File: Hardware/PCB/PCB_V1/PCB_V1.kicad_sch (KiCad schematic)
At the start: 33 parts, among them J1 Conn_01x03, J1_Afficheur Conn_01x10, J2 Conn_01x03, J3 Conn_ST_STDC14, J4 Conn_01x02, J5 Conn_01x02, J6 DIN-5_180degree, J7 Conn_01x07, U1 STM32G431KBTx, U2 MCP6002-xSN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

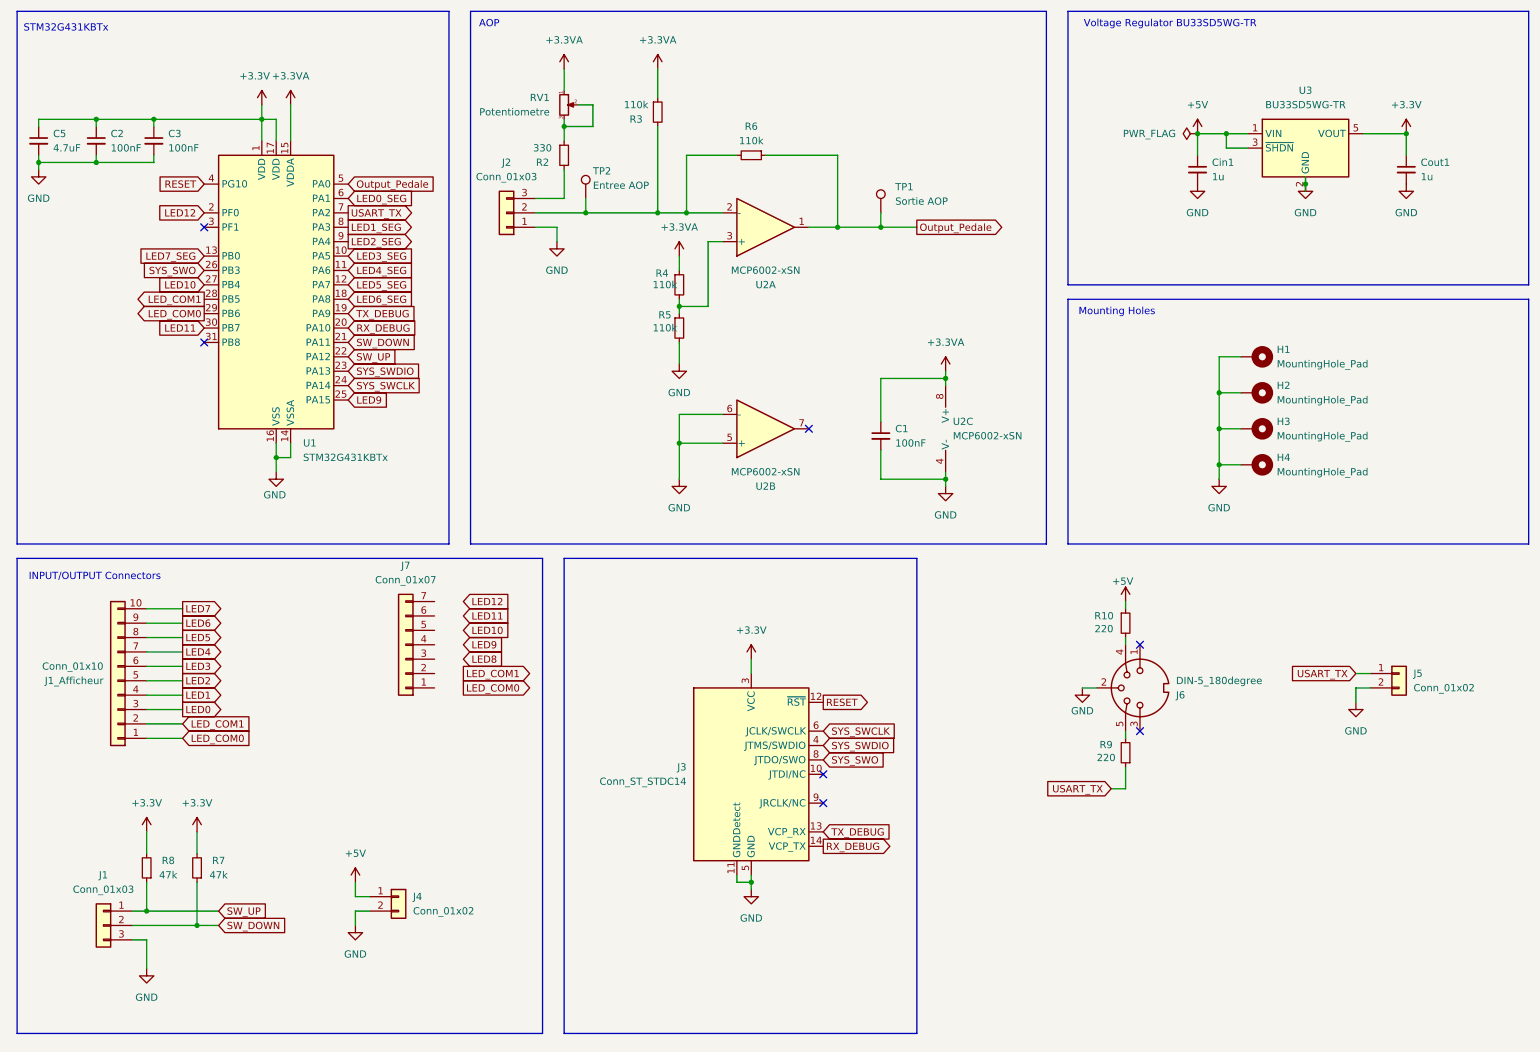
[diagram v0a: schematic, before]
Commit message: ajout transistors LED
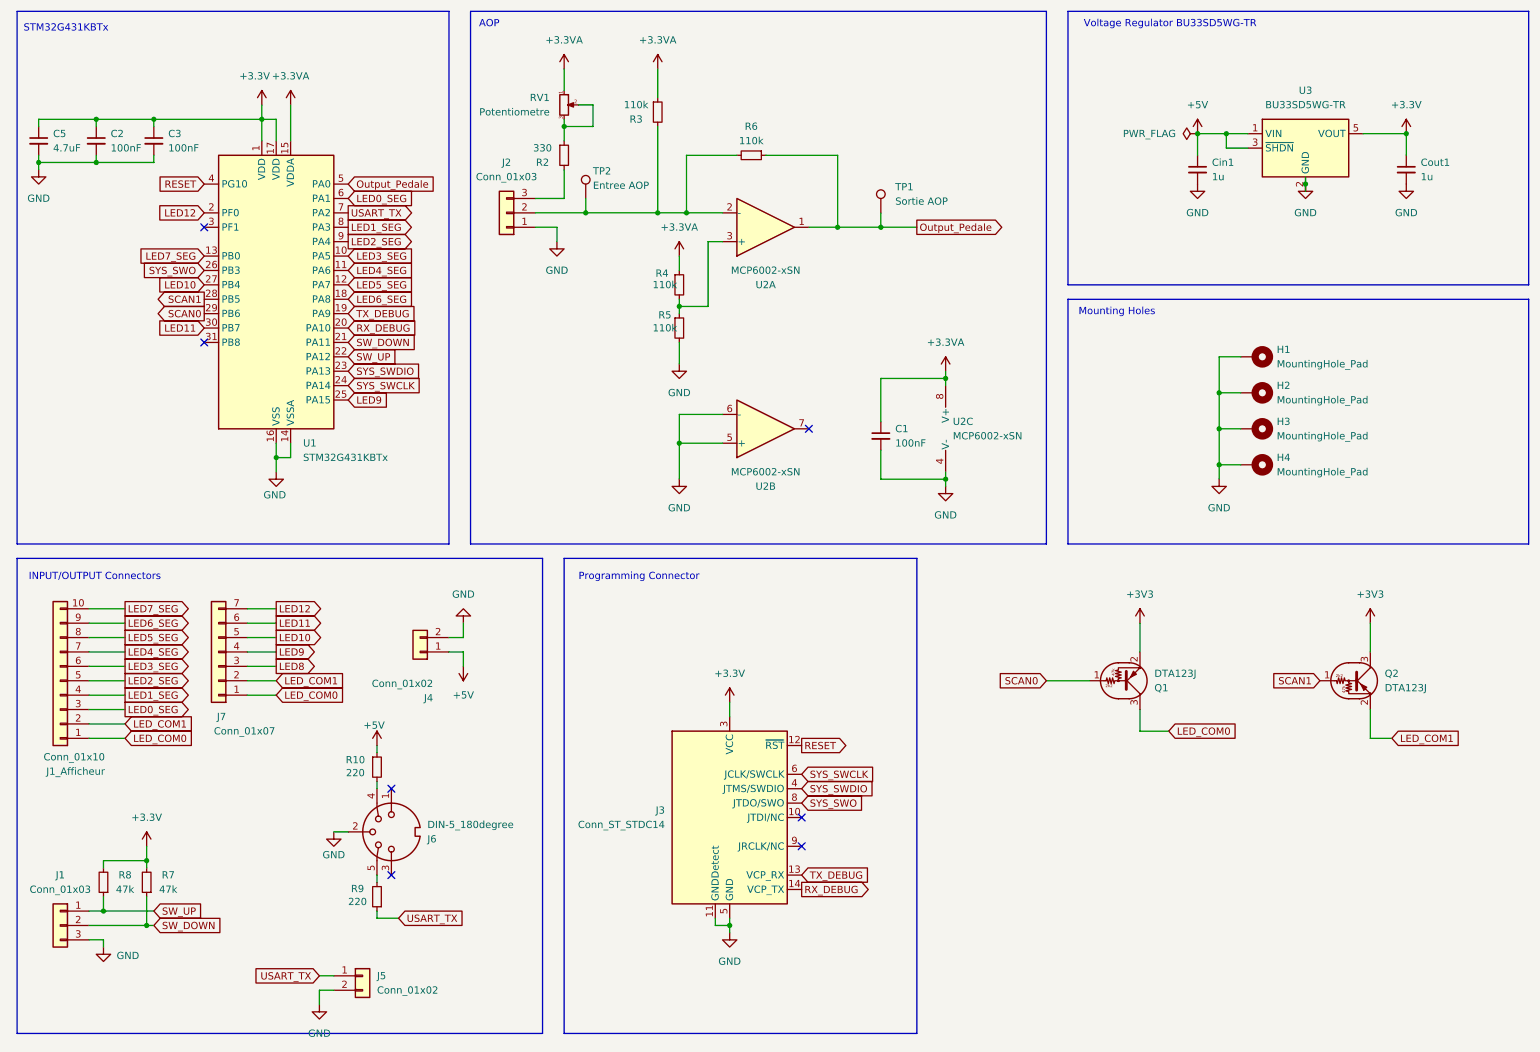
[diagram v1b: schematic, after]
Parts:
- added Q1, Q2: DTA123J, symbol Transistor_BJT:DTA123J
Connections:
- net LED0 is gone; now on net LED0_SEG: J1_Afficheur.3 (Pin_3)
- net LED1 is gone; now on net LED1_SEG: J1_Afficheur.4 (Pin_4)
- net LED2 is gone; now on net LED2_SEG: J1_Afficheur.5 (Pin_5)
- net LED3 is gone; now on net LED3_SEG: J1_Afficheur.6 (Pin_6)
- net LED4 is gone; now on net LED4_SEG: J1_Afficheur.7 (Pin_7)
- net LED5 is gone; now on net LED5_SEG: J1_Afficheur.8 (Pin_8)
- net LED6 is gone; now on net LED6_SEG: J1_Afficheur.9 (Pin_9)
- net LED7 is gone; now on net LED7_SEG: J1_Afficheur.10 (Pin_10)
- net LED10: now also J7.5 (Pin_5)
- net LED11: now also J7.6 (Pin_6)
- net LED12: now also J7.7 (Pin_7)
- net LED8: now also J7.3 (Pin_3)
- net LED9: now also J7.4 (Pin_4)
- net LED_COM0: now also J7.1 (Pin_1), Q1.3 (C); no longer U1.29 (PB6)
- net LED_COM1: now also J7.2 (Pin_2), Q2.2 (E); no longer U1.28 (PB5)
- new net +3V3: Q1.2 (E), Q2.3 (C)
- new net SCAN0: Q1.1 (B), U1.29 (PB6)
- new net SCAN1: Q2.1 (B), U1.28 (PB5)
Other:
- note added: "Programming Connector"
- moved on the sheet: J1, J1_Afficheur, J3, J4, J5, J6, J7, R10, R7, R8, R9

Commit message: Mis à jour schématique
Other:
- note added: "Transistors"
- company: (none) -> ENSEA
- title: (none) -> 1A1B Projet Pedale
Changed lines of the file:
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@@
 	(generator_version "8.0")
 	(paper "A4")
+	(title_block
+		(title "1A1B Projet Pedale")
+		(date "2025-03-11")
+		(rev "1.0")
+		(company "ENSEA")
+		(comment 1 "CHERIFI Sacha")
+		(comment 2 "TURGUT Iprahim")
+		(comment 3 "PREVOST Alexian")
+	)
 	(junction
 		(at 140.97 176.53)
@@
 		)
 	)
+	(rectangle
+		(start 177.8 111.76)
+		(end 275.59 161.29)
+		(stroke
+			(width 0)
+			(type default)
+		)
+		(fill
+			(type none)
+		)
+	)
 	(text "AOP\n"
 		(exclude_from_sim no)
@@
 		)
 	)
+	(text "Transistors"
+		(exclude_from_sim no)
+		(at 184.15 114.046 0)
+		(effects
+			(font
+				(size 1.27 1.27)
+			)
+		)
+	)
 	(text "Programming Connector\n"
 		(exclude_from_sim no)
@@
 		)
 		(instances
-			(project ""
+			(project "PCB_V1"
 				(path "/56432b71-0851-4531-93d8-c32e80e88a85"
 					(reference "#PWR024")
@@
 		)
 		(instances
-			(project ""
+			(project "PCB_V1"
 				(path "/56432b71-0851-4531-93d8-c32e80e88a85"
 					(reference "#PWR025")
@@
 		)
 		(instances
-			(project ""
+			(project "PCB_V1"
 				(path "/56432b71-0851-4531-93d8-c32e80e88a85"
 					(reference "Q1")
@@
 		)
 		(instances
-			(project ""
+			(project "PCB_V1"
 				(path "/56432b71-0851-4531-93d8-c32e80e88a85"
 					(reference "J7")
@@
 		)
 		(instances
-			(project ""
+			(project "PCB_V1"
 				(path "/56432b71-0851-4531-93d8-c32e80e88a85"
 					(reference "#PWR027")
@@
 		)
 		(instances
-			(project ""
+			(project "PCB_V1"
 				(path "/56432b71-0851-4531-93d8-c32e80e88a85"
 					(reference "C2")
@@
 		)
 		(instances
-			(project ""
+			(project "PCB_V1"
 				(path "/56432b71-0851-4531-93d8-c32e80e88a85"
 					(reference "#PWR026")
@@
 		)
 		(instances
-			(project ""
+			(project "PCB_V1"
 				(path "/56432b71-0851-4531-93d8-c32e80e88a85"
 					(reference "TP1")
@@
 		)
 		(instances
-			(project ""
+			(project "PCB_V1"
 				(path "/56432b71-0851-4531-93d8-c32e80e88a85"
 					(reference "#PWR010")
@@
 		)
 		(instances
-			(project ""
+			(project "PCB_V1"
 				(path "/56432b71-0851-4531-93d8-c32e80e88a85"
 					(reference "#PWR020")
@@
 		)
 		(instances
-			(project ""
+			(project "PCB_V1"
 				(path "/56432b71-0851-4531-93d8-c32e80e88a85"
 					(reference "J3")
@@
 		)
 		(instances
-			(project ""
+			(project "PCB_V1"
 				(path "/56432b71-0851-4531-93d8-c32e80e88a85"
 					(reference "#PWR023")
@@
 		)
 		(instances
-			(project ""
+			(project "PCB_V1"
 				(path "/56432b71-0851-4531-93d8-c32e80e88a85"
 					(reference "J4")
@@
 		)
 		(instances
-			(project ""
+			(project "PCB_V1"
 				(path "/56432b71-0851-4531-93d8-c32e80e88a85"
 					(reference "J6")
@@
 		)
 		(instances
-			(project ""
+			(project "PCB_V1"
 				(path "/56432b71-0851-4531-93d8-c32e80e88a85"
 					(reference "RV1")
@@
 		)
 		(instances
-			(project ""
+			(project "PCB_V1"
 				(path "/56432b71-0851-4531-93d8-c32e80e88a85"
 					(reference "#PWR09")
@@
 		)
 		(instances
-			(project ""
+			(project "PCB_V1"
 				(path "/56432b71-0851-4531-93d8-c32e80e88a85"
 					(reference "J1")

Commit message: ajout library footprint DIN5
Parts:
- added C5: 1uF, Capacitor_SMD:C_0603_1608Metric, symbol Device:C_Small
- added C6: 10nF, Capacitor_SMD:C_0402_1005Metric, symbol Device:C_Small
- added H5, H6: MountingHole_Pad, MountingHole:MountingHole_4mm_Pad_TopBottom, symbol Mechanical:MountingHole_Pad
- added L1: 39n, Inductor_SMD:L_0603_1608Metric, symbol Device:L_Small
- C1: footprint (none) -> Capacitor_SMD:C_0402_1005Metric
- C2: renamed from C5; footprint (none) -> Capacitor_SMD:C_0603_1608Metric
- C3: renamed from C2; footprint (none) -> Capacitor_SMD:C_0402_1005Metric
- C4: renamed from C3; footprint (none) -> Capacitor_SMD:C_0402_1005Metric
- Cin1, Cout1: value 1u -> 1uF; footprint (none) -> Capacitor_SMD:C_0603_1608Metric
- H1, H2, H3, H4: footprint (none) -> MountingHole:MountingHole_4mm_Pad_TopBottom
- J1, J2: footprint (none) -> Connector_JST:JST_XH_B3B-XH-A_1x03_P2.50mm_Vertical
- J4, J5: footprint Connector_JST:JST_XH_S2B-XH-A_1x02_P2.50mm_Horizontal -> Connector_JST:JST_XH_B2B-XH-A_1x02_P2.50mm_Vertical
- J7: footprint (none) -> Connector_JST:JST_XH_B7B-XH-A_1x07_P2.50mm_Vertical
- J8_afficheur1: renamed from J1_Afficheur; footprint (none) -> Connector_JST:JST_XH_B10B-XH-A_1x10_P2.50mm_Vertical
- Q1, Q2: footprint (none) -> Package_TO_SOT_SMD:SOT-23-3
- R10, R2, R3, R4, R5, R6, R7, R8, R9: footprint (none) -> Resistor_SMD:R_0402_1005Metric
- RV1: value Potentiometre -> 470; footprint (none) -> Potentiometer_SMD:Potentiometer_Bourns_3314J_Vertical
- U2: footprint (none) -> Package_SO:SOIC-8_3.9x4.9mm_P1.27mm
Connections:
- net +3.3V: now also L1.1
- net +3.3VA: now also C5.1, C6.1, L1.2
- net +3V3: now also Q2.2 (E); no longer Q2.3 (C)
- net GND: now also C5.2, C6.2, H5.1, H6.1
- net LED_COM1: now also Q2.3 (C); no longer Q2.2 (E)
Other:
- moved on the sheet: C2, C3, C4, Cin1, Cout1, H1, H2, H3, H4, J3, J5, Q1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

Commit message: pcb complet
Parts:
- removed H6: MountingHole_Pad, MountingHole:MountingHole_4mm_Pad_TopBottom, symbol Mechanical:MountingHole_Pad
- removed J6: DIN-5_180degree, symbol Connector:DIN-5_180degree
- added D1, D2: LED, LED_SMD:LED_0603_1608Metric, symbol Device:LED
- added J8: PRT-09536, symbol PRT-09536:PRT-09536
- added JP1: SolderJumper1, Jumper:SolderJumper-2_P1.3mm_Open_TrianglePad1.0x1.5mm, symbol Jumper:SolderJumper_2_Open
- added JP2: SolderJumper, Jumper:SolderJumper-2_P1.3mm_Open_TrianglePad1.0x1.5mm, symbol Jumper:SolderJumper_2_Open
- added R1, R11: 1000, Resistor_SMD:R_0402_1005Metric, symbol Device:R_Small
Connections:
- net +3V3 is gone; now on net +3.3V: Q1.2 (E), Q2.2 (E)
- net +3.3V: now also D1.2 (A)
- net +5V: now also R10.2; no longer R10.1
- net GND: now also J8.2, J8.E1, J8.E2, R1.1, R11.1
- net at R9.2: now also JP2.1 (A)
- net at U1.31 (PB8): now also D2.2 (A)
- new net: J8.4, JP1.1 (A)
- new net: J8.5, JP2.2 (B)
- new net: JP1.2 (B), R10.1
- new net: D2.1 (K), R11.2
- new net: D1.1 (K), R1.2
- no-connect marks 7 -> 6
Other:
- moved on the sheet: Cin1, Cout1, J1, R10, R7, R8, R9, U1, U3
